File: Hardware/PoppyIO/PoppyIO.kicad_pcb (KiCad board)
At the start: 2 copper layers, 102 x 86 mm, 244 parts, among them J1 WAGO 233-504, J10 Phoenix MPT 0,5/ 4-2,54, J11 TC2030-IDC, J12 Conn_02x06_Odd_Even, J2 WAGO 233-504, J3 WAGO 233-504, J4 WAGO 233-504, J5 WAGO 233-504, J6 WAGO 233-504, J7 WAGO 233-504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

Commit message: hw: io: PCB layout
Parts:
- JP10, JP3, JP4, JP5, JP6, JP7, JP8, JP9, U2, U3, U4, U5: moved to B.Cu
- moved JP8 329.2 mm to (113.2, 108.9), turned to 180 degrees
- moved JP7 321.9 mm to (113.2, 111.4), turned to 180 degrees
- moved JP4 315.6 mm to (113.2, 96.2), turned to 180 degrees
- moved JP10 311.1 mm to (138.6, 108.9), turned to 180 degrees
- moved JP3 309.1 mm to (113.2, 98.7), turned to 180 degrees
- moved JP9 303.2 mm to (138.6, 111.4), turned to 180 degrees
- moved JP6 296.0 mm to (138.6, 96.2), turned to 180 degrees
- moved JP5 290.1 mm to (138.6, 98.7), turned to 180 degrees
- moved U2 271.3 mm to (119.5, 93.7)
- moved R3 250.4 mm to (119.5, 92.4)
- moved R4 250.3 mm to (145.2, 97.2)
- moved C6 248.6 mm to (116.7, 102.5)
- moved C4 243.5 mm to (119.5, 90.6)
- moved U3 236.1 mm to (144.9, 93.7)
- moved C5 236.1 mm to (145.2, 99.0)
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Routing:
- net +3V3: track 0.00 -> 119.7 mm, vias 0 -> 4
- net GND: track 0.00 -> 93.9 mm, vias 0 -> 40
- net /O07_LOGIC: track 0.00 -> 31.0 mm, vias 0 -> 1
- net /O00_LOGIC: track 0.00 -> 30.1 mm, vias 0 -> 1
- net /O01_LOGIC: track 0.00 -> 28.2 mm, vias 0 -> 1
- net /O06_LOGIC: track 0.00 -> 28.2 mm, vias 0 -> 1
- net /O15_LOGIC: track 0.00 -> 27.3 mm, vias 0 -> 1
- net /O05_LOGIC: track 0.00 -> 26.5 mm, vias 0 -> 1
- net /O08_LOGIC: track 0.00 -> 25.8 mm, vias 0 -> 1
- net /O13_LOGIC: track 0.00 -> 25.5 mm, vias 0 -> 1
- net /O14_LOGIC: track 0.00 -> 25.1 mm, vias 0 -> 1
- net /O09_LOGIC: track 0.00 -> 24.8 mm, vias 0 -> 1
- net /O02_LOGIC: track 0.00 -> 24.6 mm, vias 0 -> 1
- net /O12_LOGIC: track 0.00 -> 24.1 mm, vias 0 -> 1
- net /O10_LOGIC: track 0.00 -> 23.0 mm, vias 0 -> 1
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- added copper zone on B.Cu, net GND

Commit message: hw: io: More PCB layout
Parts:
- C4, C5, C6, C7, JP11, JP2: moved to B.Cu
- moved SW1 328.6 mm to (167.8, 115.2), turned to -90 degrees
- moved C28 316.0 mm to (163.5, 112.2), turned to 90 degrees
- moved R1 311.8 mm to (167.8, 88.1), turned to 180 degrees
- moved JP1 309.2 mm to (162.1, 74.6), turned to 90 degrees
- moved R70 307.8 mm to (169.6, 108.4), turned to 90 degrees
- moved C2 294.2 mm to (167.8, 89.6), turned to 180 degrees
- moved D2 293.3 mm to (190.6, 62.5), turned to 180 degrees
- moved C3 293.3 mm to (167.8, 91.1), turned to 180 degrees
- moved D1 292.4 mm to (190.6, 59.4), turned to 180 degrees
- moved R2 287.1 mm to (167.8, 92.6), turned to 180 degrees
- moved JP11 280.4 mm to (168.0, 111.9), turned to -90 degrees
- moved C1 274.0 mm to (190.6, 67.0), turned to -90 degrees
- moved U1 273.4 mm to (186.2, 117.5), turned to 180 degrees
- moved JP2 257.5 mm to (172.6, 131.5), turned to 180 degrees
- moved TP36 255.6 mm to (163.0, 115.2)
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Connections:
- J9 pad 1: +5V -> GND
- J9 pad 2: +5V -> GND
- J9 pad 3: GND -> +5V
- J9 pad 4: GND -> +5V
- JP1 pad 1: +3V3 -> +5V
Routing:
- net +3V3: track 119.7 -> 411.0 mm, vias 4 -> 25
- net GND: track 93.9 -> 279.0 mm, vias 40 -> 56
- net IO_~{RESET}: track 16.1 -> 120.2 mm, vias 2 -> 8
- net IO_SDA: track 17.1 -> 101.3 mm, vias 2 -> 8
- net IO_SCL: track 16.9 -> 100.3 mm, vias 2 -> 8
- net +24V: track 0.00 -> 70.2 mm
- net /~{RESET}: track 0.00 -> 54.2 mm, vias 0 -> 1
- net IO_INT0: track 15.2 -> 66.5 mm, vias 2 -> 4
- net IO_INT1: track 0.00 -> 30.0 mm, vias 0 -> 4
- net /SWCLK: track 0.00 -> 23.8 mm, vias 0 -> 1
- net /SWDIO: track 0.00 -> 19.5 mm, vias 0 -> 1
- net Net-(J12-Pad3): track 0.00 -> 19.1 mm, vias 0 -> 1
- net Net-(F1-Pad1): track 0.00 -> 15.5 mm, vias 0 -> 1
- net Net-(F8-Pad1): track 0.00 -> 7.92 mm, vias 0 -> 1
- net Net-(F2-Pad1): track 0.00 -> 7.92 mm, vias 0 -> 1
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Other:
- board text added: "+24V"
- board text added: "+5V"
- board text added: "GND"

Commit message: hw: io: Update PCB
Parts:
- moved J12 15.2 mm to (166.5, 77.1)
- moved JP1 13.6 mm to (174.1, 68.2), turned to 180 degrees
- moved D1 13.1 mm to (178.6, 64.4), turned to -90 degrees
- moved D2 9.09 mm to (181.8, 64.4), turned to -90 degrees
- moved C1 4.26 mm to (186.4, 66.2), turned to 0 degrees
- moved C27 1.78 mm to (167.8, 85.8)
- moved R69 1.78 mm to (167.8, 84.3)
- moved R73 1.78 mm to (169.6, 82.7)
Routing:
- net /VSYS: track 0.00 -> 93.2 mm
- net IO_SCL: track 100.3 -> 146.0 mm, vias 8 -> 11
- net IO_SDA: track 101.3 -> 145.7 mm, vias 8 -> 11
- net +3V3: track 411.0 -> 453.6 mm, vias 25 -> 29
- net +5V: track 0.00 -> 38.6 mm, vias 0 -> 1
- net Net-(C2-Pad1): track 1.54 -> 31.4 mm, vias 0 -> 2
- net IO_INT1: track 30.0 -> 57.2 mm, vias 4 -> 6
- net Net-(C3-Pad1): track 1.54 -> 25.2 mm, vias 0 -> 2
- net PICO_TX: track 0.00 -> 22.5 mm
- net PICO_RX: track 0.00 -> 22.3 mm
- net IO_INT0: track 66.5 -> 88.3 mm, vias 4 -> 8
- net Net-(J12-Pad3): track 19.1 -> 6.14 mm, vias 1 -> 0
- net IO_~{RESET}: track 120.2 -> 131.8 mm, vias 8 -> 10
- net Net-(D1-Pad2): track 0.00 -> 7.92 mm
- net GND: track 279.0 -> 283.9 mm, vias 56 -> 99
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- added copper zone on F.Cu, net GND

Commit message: hw: io: Updae PCB and DRC fixes
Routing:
- net GND: track 283.9 -> 337.0 mm, vias 99 -> 112
- net +3V3: track 453.6 -> 456.5 mm, vias 29 -> 30
- net Net-(C20-Pad1): track 16.7 -> 18.3 mm, vias 2 -> 3
- net Net-(C23-Pad1): track 12.2 -> 13.8 mm, vias 0 -> 1
- net Net-(C22-Pad1): track 16.7 -> 18.3 mm, vias 2 -> 3
- net Net-(C21-Pad1): track 16.7 -> 18.3 mm, vias 2 -> 3
- net /O01_LOGIC: track 28.2 -> 27.1 mm
- net /O02_LOGIC: track 24.6 -> 23.9 mm
- net (no net): vias 2 -> 0

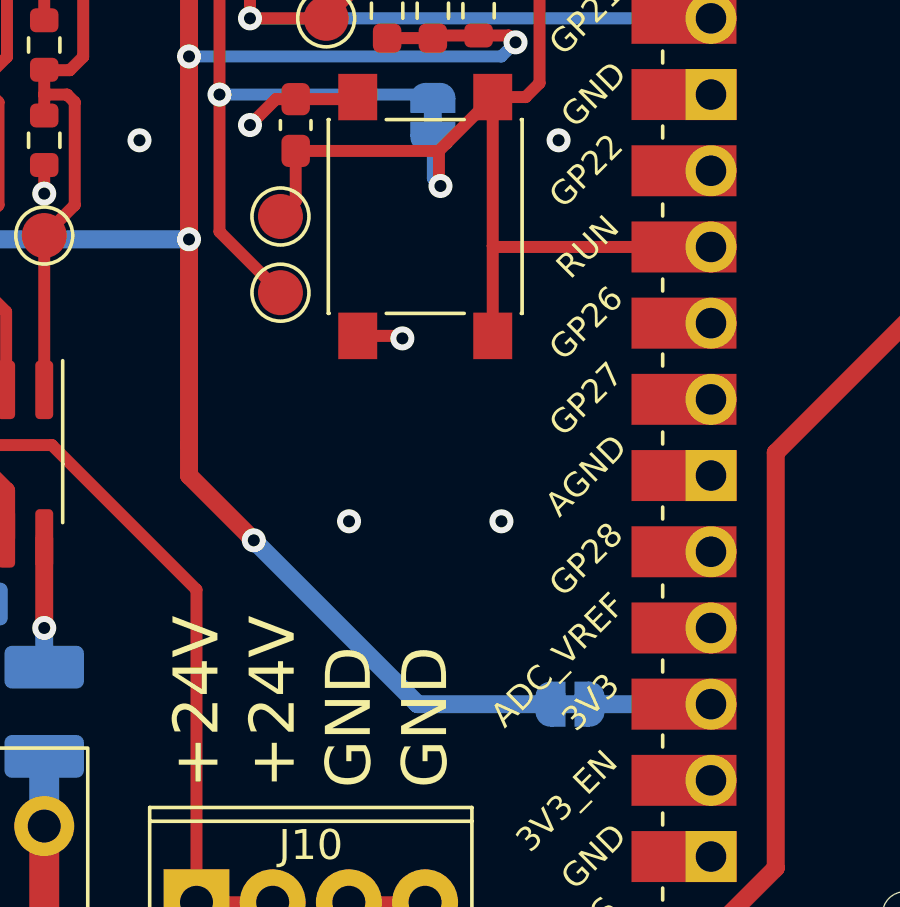
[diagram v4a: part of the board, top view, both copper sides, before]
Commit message: hw: io: Update JP2
shouldn't be a solder jumper
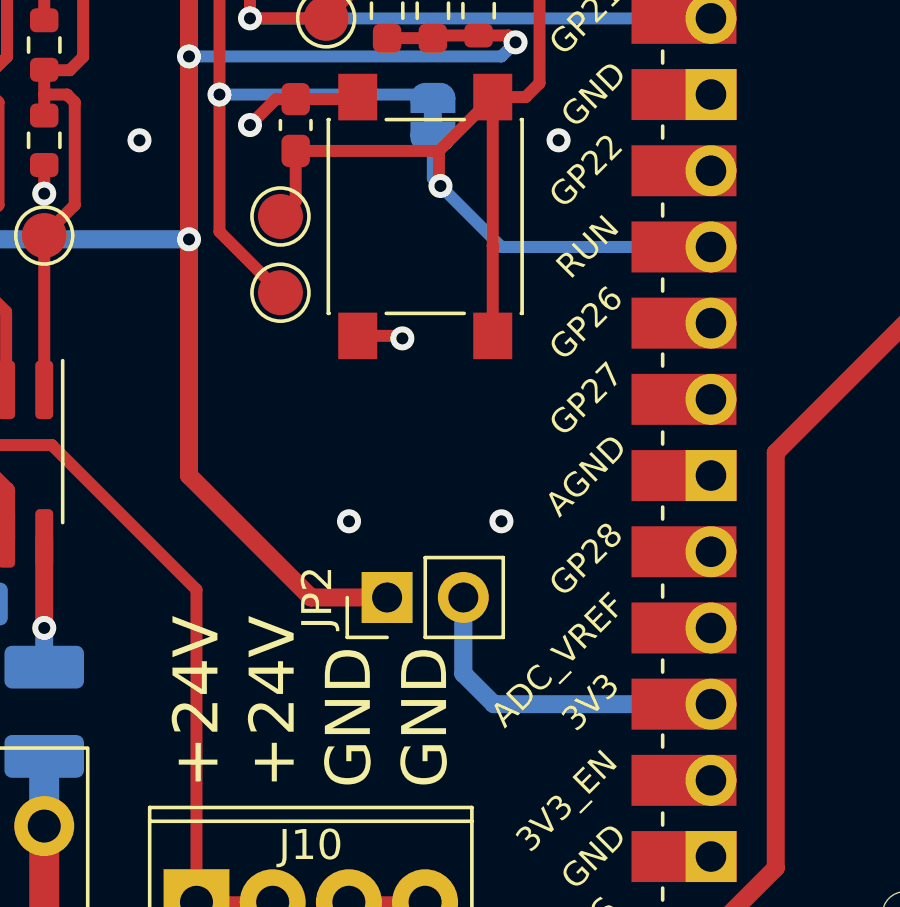
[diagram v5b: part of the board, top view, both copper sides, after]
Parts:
- JP2: value SolderJumper_2_Bridged -> ~; footprint Jumper:SolderJumper-2_P1.3mm_Bridged_RoundedPad1.0x1.5mm -> Connector_PinHeader_2.54mm:PinHeader_1x02_P2.54mm_Vertical; moved to F.Cu
- moved JP2 7.06 mm to (166.5, 127.9), turned to 90 degrees
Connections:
- JP2 pad 1: Net-(JP2-Pad1) -> +3V3
- JP2 pad 2: +3V3 -> Net-(U1-Pad36)
- U1 pad 36: Net-(JP2-Pad1) -> Net-(U1-Pad36)
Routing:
- net Net-(U1-Pad36): track 0.00 -> 11.2 mm
- net +3V3: track 456.5 -> 449.6 mm, vias 30 -> 29
- net Net-(JP2-Pad1): track 4.05 -> 0.00 mm
- net /~{RESET}: track 54.2 -> 56.8 mm

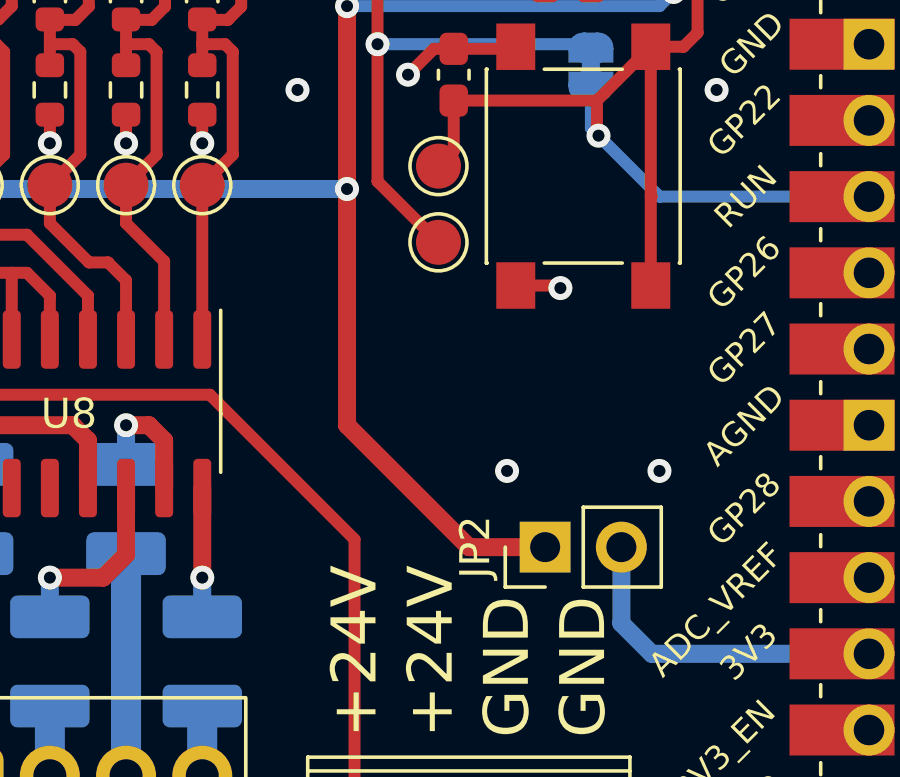
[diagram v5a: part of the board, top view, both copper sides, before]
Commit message: hw: io: Add footprints for 3V3 decoupling caps
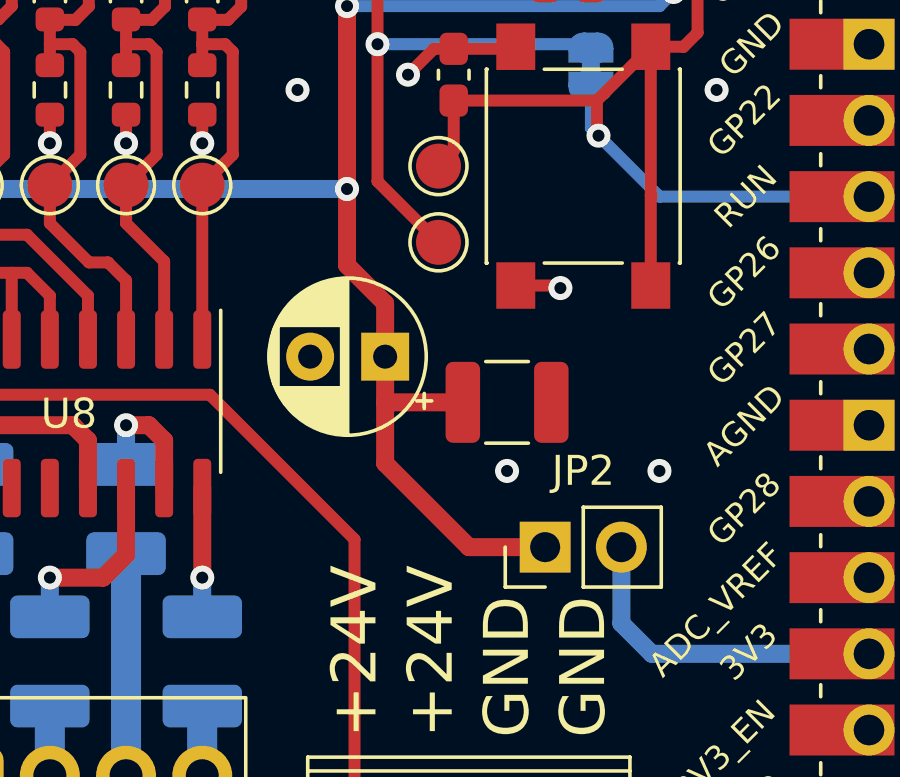
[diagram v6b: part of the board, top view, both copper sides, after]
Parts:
- added C30: 10u, Capacitor_SMD:C_1210_3225Metric, F.Cu at (165.2, 123.1)
- added C31: 10u, Capacitor_THT:CP_Radial_D5.0mm_P2.50mm, F.Cu at (161.2, 121.6)
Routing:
- net +3V3: track 449.6 -> 452.2 mm

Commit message: hw: io: Add artwork
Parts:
- added REF**: ESD-Logo_6.6x6mm_SilkScreen, Symbol:ESD-Logo_6.6x6mm_SilkScreen, F.Cu at (195.1, 63.8)
- added REF**: WEEE-Logo_5.6x8mm_SilkScreen, Symbol:WEEE-Logo_5.6x8mm_SilkScreen, B.Cu at (186.8, 84.8)
- added REF**: ESD-Logo_6.6x6mm_SilkScreen, Symbol:ESD-Logo_6.6x6mm_SilkScreen, B.Cu at (194.4, 84.8)
- added REF**: KiCad-Logo_8mm_SilkScreen, Symbol:KiCad-Logo_8mm_SilkScreen, B.Cu at (186.2, 119.7)
- added SYM1: SYM_Rahix, PoppyLogicController:SYM_Rahix, F.Cu at (185.6, 86.0)
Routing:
- net GND: vias 112 -> 107
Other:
- board text added: "Poppy Logic Controller - IO"
- board text added: "Rahix 2022-04-23"
- board text added: "Serial:"
